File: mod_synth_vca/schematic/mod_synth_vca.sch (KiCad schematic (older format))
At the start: 46 parts, among them J1 Conn_02x08_Odd_Even, J2 AudioJack2, J3 AudioJack2, J4 AudioJack2, J5 AudioJack2, J6 AudioJack2, J7 AudioJack2, J8 Conn_01x10_Female, J9 Conn_01x10_Male, U1 TL074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

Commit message: Modify pcb layout
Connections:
- net PCB_A_CV_A1: now also J9.8 (Pin_8); no longer J9.2 (Pin_2)
- net PCB_A_OUT_A: now also J9.9 (Pin_9); no longer J9.6 (Pin_6)
- net PCB_A_OUT_B: now also J9.2 (Pin_2); no longer J9.7 (Pin_7)
- net PCB_A_VOL_A: now also J9.7 (Pin_7); no longer J9.4 (Pin_4)
- net PCB_A_VOL_B: now also J9.4 (Pin_4); no longer J9.5 (Pin_5)
- net PCB_B_CV_A1: now also J8.8 (Pin_8); no longer J8.2 (Pin_2)
- net PCB_B_OUT_A: now also J8.9 (Pin_9); no longer J8.6 (Pin_6)
- net PCB_B_OUT_B: now also J8.2 (Pin_2); no longer J8.7 (Pin_7)
- net PCB_B_VOL_A: now also J8.7 (Pin_7); no longer J8.4 (Pin_4)
- net PCB_B_VOL_B: now also J8.4 (Pin_4); no longer J8.5 (Pin_5)
- net PCB_B_IN_A: now reaches R12.1, U3.2 (-)
- net PCB_B_IN_A: now also J8.6 (Pin_6); no longer R9.1
- net PCB_B_IN_B: now reaches R11.1, U2.2 (-)
- net PCB_B_IN_B: now also J8.5 (Pin_5); no longer R5.1
- new net PCB_A_IN_A: J9.6 (Pin_6), R9.1
- new net PCB_A_IN_B: J9.5 (Pin_5), R5.1
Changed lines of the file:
@@
-$Comp
-L Amplifier_Operational:TL074 U1
-U 3 1 5D3B02E4
-P 5600 4325
-F 0 "U1" H 5600 4692 50  0000 C CNN
-F 1 "TL074" H 5600 4601 50  0000 C CNN
-F 2 "Package_DIP:DIP-14_W7.62mm_Socket_LongPads" H 5550 4425 50  0001 C CNN
-F 3 "http://www.ti.com/lit/ds/symlink/tl071.pdf" H 5650 4525 50  0001 C CNN
-	3    5600 4325
-	1    0    0    -1
-$EndComp
-$Comp
-L Amplifier_Operational:TL074 U1
-U 4 1 5D3B1A55
-P 7650 4725
-F 0 "U1" H 7650 5092 50  0000 C CNN
-F 1 "TL074" H 7650 5001 50  0000 C CNN
-F 2 "Package_DIP:DIP-14_W7.62mm_Socket_LongPads" H 7600 4825 50  0001 C CNN
-F 3 "http://www.ti.com/lit/ds/symlink/tl071.pdf" H 7700 4925 50  0001 C CNN
-	4    7650 4725
-	1    0    0    -1
-$EndComp
 $Comp
 L Amplifier_Operational:TL074 U1
@@
 	4250 2925 3900 2925
 Wire Wire Line
-	4825 2150 5250 2150
-Wire Wire Line
-	5250 2150 5250 2300
+	4825 2150 5000 2150
 Wire Wire Line
 	5250 2300 5325 2300
@@
 $EndComp
 $Comp
-L power:GND #PWR0124
-U 1 1 5D3DA57A
-P 7175 4350
-F 0 "#PWR0124" H 7175 4100 50  0001 C CNN
-F 1 "GND" H 7180 4177 50  0000 C CNN
-F 2 "" H 7175 4350 50  0001 C CNN
-F 3 "" H 7175 4350 50  0001 C CNN
-	1    7175 4350
-	-1   0    0    1
-$EndComp
-$Comp
 L Connector:AudioJack2 J2
 U 1 1 5D3DA584
@@
 	4200 5800 3850 5800
 Wire Wire Line
-	4775 5025 5200 5025
-Wire Wire Line
-	5200 5025 5200 5175
+	4775 5025 5000 5025
 Wire Wire Line
 	5200 5175 5275 5175
@@
 Wire Wire Line
 	5550 6175 5550 5975
-$Comp
-L power:GND #PWR0125
-U 1 1 5D3DA5C9
-P 5125 4025
-F 0 "#PWR0125" H 5125 3775 50  0001 C CNN
-F 1 "GND" H 5130 3852 50  0000 C CNN
-F 2 "" H 5125 4025 50  0001 C CNN
-F 3 "" H 5125 4025 50  0001 C CNN
-	1    5125 4025
-	-1   0    0    1
-$EndComp
-Wire Wire Line
-	5125 4025 5125 4225
-Wire Wire Line
-	5125 4225 5300 4225
 Wire Wire Line
 	4775 3775 4950 3775
-Wire Wire Line
-	7175 4350 7175 4625
-Wire Wire Line
-	7175 4625 7350 4625
-$Comp
-L Device:D D1
-U 1 1 5D3DA5DC
-P 6200 4475
-F 0 "D1" V 6246 4396 50  0000 R CNN
-F 1 "1N4148" V 6155 4396 50  0000 R CNN
-F 2 "Diode_THT:D_DO-35_SOD27_P7.62mm_Horizontal" H 6200 4475 50  0001 C CNN
-F 3 "~" H 6200 4475 50  0001 C CNN
-	1    6200 4475
-	0    -1   -1   0
-$EndComp
-Wire Wire Line
-	6200 4625 5125 4625
-Wire Wire Line
-	5125 4625 5125 4425
-Wire Wire Line
-	6200 4625 6475 4625
-Wire Wire Line
-	6475 4625 6475 4650
-Connection ~ 6200 4625
 $Comp
 L Device:CP C1
@@
 Connection ~ 8125 5275
 Wire Wire Line
-	7350 4825 7175 4825
-Wire Wire Line
-	7175 4825 7175 5275
-Wire Wire Line
 	7950 4725 8125 4725
 Wire Wire Line
@@
 Wire Wire Line
 	6175 5275 7175 5275
-Wire Wire Line
-	6475 4975 6475 4950
-Wire Wire Line
-	5875 4975 6475 4975
-$Comp
-L Device:D D3
-U 1 1 5D3DA614
-P 6475 4800
-F 0 "D3" V 6521 4721 50  0000 R CNN
-F 1 "1N4148" V 6430 4721 50  0000 R CNN
-F 2 "Diode_THT:D_DO-35_SOD27_P7.62mm_Horizontal" H 6475 4800 50  0001 C CNN
-F 3 "~" H 6475 4800 50  0001 C CNN
-	1    6475 4800
-	0    -1   -1   0
-$EndComp
-$Comp
-L power:+12V #PWR0127
-U 1 1 5D3DA61E
-P 5550 4825
-F 0 "#PWR0127" H 5550 4675 50  0001 C CNN
-F 1 "+12V" H 5565 4998 50  0000 C CNN
-F 2 "" H 5550 4825 50  0001 C CNN
-F 3 "" H 5550 4825 50  0001 C CNN
-	1    5550 4825
-	0    -1   -1   0
-$EndComp
 $Comp
 L power:GND #PWR0128
@@
 	1    0    0    -1
 $EndComp
-$Comp
-L Amplifier_Operational:CA3080 U2
-U 1 1 5D3DA632
-P 5875 5275
-F 0 "U2" H 6219 5321 50  0000 L CNN
-F 1 "CA3080" H 6219 5230 50  0000 L CNN
-F 2 "Package_DIP:DIP-8_W7.62mm_Socket_LongPads" H 5875 5275 50  0001 C CNN
-F 3 "http://www.intersil.com/content/dam/Intersil/documents/ca30/ca3080-a.pdf" H 5875 5375 50  0001 C CNN
-	1    5875 5275
-	1    0    0    -1
-$EndComp
-Wire Wire Line
-	5775 4825 5775 4975
-Wire Wire Line
-	5900 4325 6200 4325
-Wire Wire Line
-	5550 4825 5775 4825
-Wire Wire Line
-	6200 4325 6875 4325
-Wire Wire Line
-	6875 4325 6875 5575
 Wire Wire Line
 	5775 5575 6875 5575
-Connection ~ 6200 4325
 $Comp
 L power:-12V #PWR0129
@@
 Wire Wire Line
 	4900 1550 5175 1550
-Text Label 4950 3775 0    50   ~ 0
-PCB_A_CV_B1
-Connection ~ 5125 4425
-Wire Wire Line
-	5125 4425 5300 4425
 Wire Wire Line
 	4775 4425 4900 4425
-Text Label 4900 4100 0    50   ~ 0
-PCB_B_CV_B1
 Wire Wire Line
 	4900 4100 4900 4425
-Connection ~ 4900 4425
-Wire Wire Line
-	4900 4425 5125 4425
-Text Label 4525 6850 0    50   ~ 0
+Text Label 4525 7450 0    50   ~ 0
 PCB_A_CV_A1
 Text Label 4525 6950 0    50   ~ 0
 PCB_A_CV_B1
-Text Label 3300 6850 2    50   ~ 0
+Text Label 3275 7450 2    50   ~ 0
 PCB_B_CV_A1
 Text Label 3300 6950 2    50   ~ 0
@@
 Wire Wire Line
 	4475 4425 4475 4675
+Text Label 4525 7350 0    50   ~ 0
+PCB_A_VOL_A
 Text Label 4525 7050 0    50   ~ 0
-PCB_A_VOL_A
-Text Label 4525 7150 0    50   ~ 0
 PCB_A_VOL_B
+Text Label 3275 7350 2    50   ~ 0
+PCB_B_VOL_A
 Text Label 3275 7050 2    50   ~ 0
-PCB_B_VOL_A
-Text Label 3275 7150 2    50   ~ 0
 PCB_B_VOL_B
 Wire Wire Line
@@
 Wire Wire Line
 	8275 5275 8275 5500
-Text Label 4525 7250 0    50   ~ 0
+Text Label 4525 7550 0    50   ~ 0
 PCB_A_OUT_A
-Text Label 4525 7350 0    50   ~ 0
+Text Label 4525 6850 0    50   ~ 0
 PCB_A_OUT_B
-Text Label 3275 7250 2    50   ~ 0
+Text Label 3275 7550 2    50   ~ 0
 PCB_B_OUT_A
-Text Label 3275 7350 2    50   ~ 0
+Text Label 3300 6850 2    50   ~ 0
 PCB_B_OUT_B
 Wire Wire Line
@@
 Text Label 8800 5600 0    50   ~ 0
 PCB_A_GND
+Text Label 5000 2100 0    50   ~ 0
+PCB_A_IN_A
+Wire Wire Line
+	5000 2100 5000 2150
+Wire Wire Line
+	5000 4975 5000 5025
+Text Label 5125 2375 2    50   ~ 0
+PCB_B_IN_A
+Text Label 5125 5275 2    50   ~ 0
+PCB_B_IN_B
+Wire Wire Line
+	5125 2375 5250 2375
+Wire Wire Line
+	5250 2375 5250 2300
+Wire Wire Line
+	5200 5175 5200 5275
+Wire Wire Line
+	5200 5275 5125 5275
+Connection ~ 4900 4425
+Text Label 5000 4975 0    50   ~ 0
+PCB_A_IN_B
+Text Label 4900 4100 0    50   ~ 0
+PCB_B_CV_B1
+Text Label 4950 3775 0    50   ~ 0
+PCB_A_CV_B1
+Wire Wire Line
+	6875 4325 6875 5575
+Wire Wire Line
+	5550 4825 5775 4825
+Wire Wire Line
+	5775 4825 5775 4975
+$Comp
+L Amplifier_Operational:CA3080 U2
+U 1 1 5D3DA632
+P 5875 5275
+F 0 "U2" H 6219 5321 50  0000 L CNN
+F 1 "CA3080" H 6219 5230 50  0000 L CNN
+F 2 "Package_DIP:DIP-8_W7.62mm_Socket_LongPads" H 5875 5275 50  0001 C CNN
+F 3 "http://www.intersil.com/content/dam/Intersil/documents/ca30/ca3080-a.pdf" H 5875 5375 50  0001 C CNN
+	1    5875 5275
+	1    0    0    -1
+$EndComp
+$Comp
+L power:+12V #PWR0127
+U 1 1 5D3DA61E
+P 5550 4825
+F 0 "#PWR0127" H 5550 4675 50  0001 C CNN
+F 1 "+12V" H 5565 4998 50  0000 C CNN
+F 2 "" H 5550 4825 50  0001 C CNN
+F 3 "" H 5550 4825 50  0001 C CNN
+	1    5550 4825
+	0    -1   -1   0
+$EndComp
+$Comp
+L Device:D D3
+U 1 1 5D3DA614
+P 6475 4800
+F 0 "D3" V 6521 4721 50  0000 R CNN
+F 1 "1N4148" V 6430 4721 50  0000 R CNN
+F 2 "Diode_THT:D_DO-35_SOD27_P7.62mm_Horizontal" H 6475 4800 50  0001 C CNN
+F 3 "~" H 6475 4800 50  0001 C CNN
+	1    6475 4800
+	0    -1   -1   0
+$EndComp
+Wire Wire Line
+	5875 4975 6475 4975
+Wire Wire Line
+	6475 4975 6475 4950
+Wire Wire Line
+	7175 4825 7175 5275
+Wire Wire Line
+	7350 4825 7175 4825
+Wire Wire Line
+	6475 4625 6475 4650
+Wire Wire Line
+	4900 4425 5125 4425
+Wire Wire Line
+	5125 4425 5300 4425
+Connection ~ 5125 4425
+Wire Wire Line
+	5125 4625 5125 4425
+Wire Wire Line
+	6200 4325 6875 4325
+Wire Wire Line
+	5900 4325 6200 4325
+Connection ~ 6200 4325
+Wire Wire Line
+	6200 4625 6475 4625
+Wire Wire Line
+	6200 4625 5125 4625
+Connection ~ 6200 4625
+$Comp
+L Device:D D1
+U 1 1 5D3DA5DC
+P 6200 4475
+F 0 "D1" V 6246 4396 50  0000 R CNN
+F 1 "1N4148" V 6155 4396 50  0000 R CNN
+F 2 "Diode_THT:D_DO-35_SOD27_P7.62mm_Horizontal" H 6200 4475 50  0001 C CNN
+F 3 "~" H 6200 4475 50  0001 C CNN
+	1    6200 4475
+	0    -1   -1   0
+$EndComp
+Wire Wire Line
+	7175 4625 7350 4625
+Wire Wire Line
+	7175 4350 7175 4625
+Wire Wire Line
+	5125 4225 5300 4225
+Wire Wire Line
+	5125 4025 5125 4225
+$Comp
+L power:GND #PWR0125
+U 1 1 5D3DA5C9
+P 5125 4025
+F 0 "#PWR0125" H 5125 3775 50  0001 C CNN
+F 1 "GND" H 5130 3852 50  0000 C CNN
+F 2 "" H 5125 4025 50  0001 C CNN
+F 3 "" H 5125 4025 50  0001 C CNN
+	1    5125 4025
+	-1   0    0    1
+$EndComp
+$Comp
+L power:GND #PWR0124
+U 1 1 5D3DA57A
+P 7175 4350
+F 0 "#PWR0124" H 7175 4100 50  0001 C CNN
+F 1 "GND" H 7180 4177 50  0000 C CNN
+F 2 "" H 7175 4350 50  0001 C CNN
+F 3 "" H 7175 4350 50  0001 C CNN
+	1    7175 4350
+	-1   0    0    1
+$EndComp
+$Comp
+L Amplifier_Operational:TL074 U1
+U 4 1 5D3B1A55
+P 7650 4725
+F 0 "U1" H 7650 5092 50  0000 C CNN
+F 1 "TL074" H 7650 5001 50  0000 C CNN
+F 2 "Package_DIP:DIP-14_W7.62mm_Socket_LongPads" H 7600 4825 50  0001 C CNN
+F 3 "http://www.ti.com/lit/ds/symlink/tl071.pdf" H 7700 4925 50  0001 C CNN
+	4    7650 4725
+	1    0    0    -1
+$EndComp
+$Comp
+L Amplifier_Operational:TL074 U1
+U 3 1 5D3B02E4
+P 5600 4325
+F 0 "U1" H 5600 4692 50  0000 C CNN
+F 1 "TL074" H 5600 4601 50  0000 C CNN
+F 2 "Package_DIP:DIP-14_W7.62mm_Socket_LongPads" H 5550 4425 50  0001 C CNN
+F 3 "http://www.ti.com/lit/ds/symlink/tl071.pdf" H 5650 4525 50  0001 C CNN
+	3    5600 4325
+	1    0    0    -1
+$EndComp
+Text Label 4525 7250 0    50   ~ 0
+PCB_A_IN_A
+Text Label 4525 7150 0    50   ~ 0
+PCB_A_IN_B
+Text Label 3275 7250 2    50   ~ 0
+PCB_B_IN_A
+Text Label 3275 7150 2    50   ~ 0
+PCB_B_IN_B
+Wire Wire Line
+	3275 7450 3650 7450
+Wire Wire Line
+	4100 7450 4525 7450
+Wire Wire Line
+	4525 7550 4100 7550
+Wire Wire Line
+	3650 7550 3275 7550
 $EndSCHEMATC

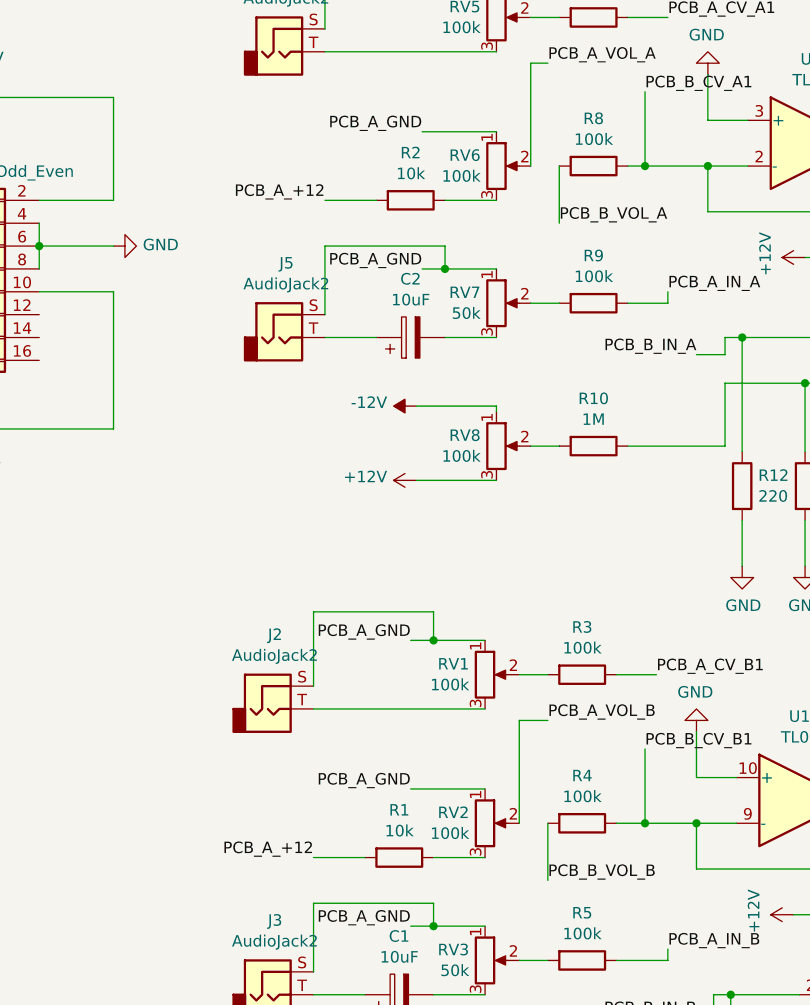
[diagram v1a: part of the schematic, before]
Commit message: Volume resistor should be 20k
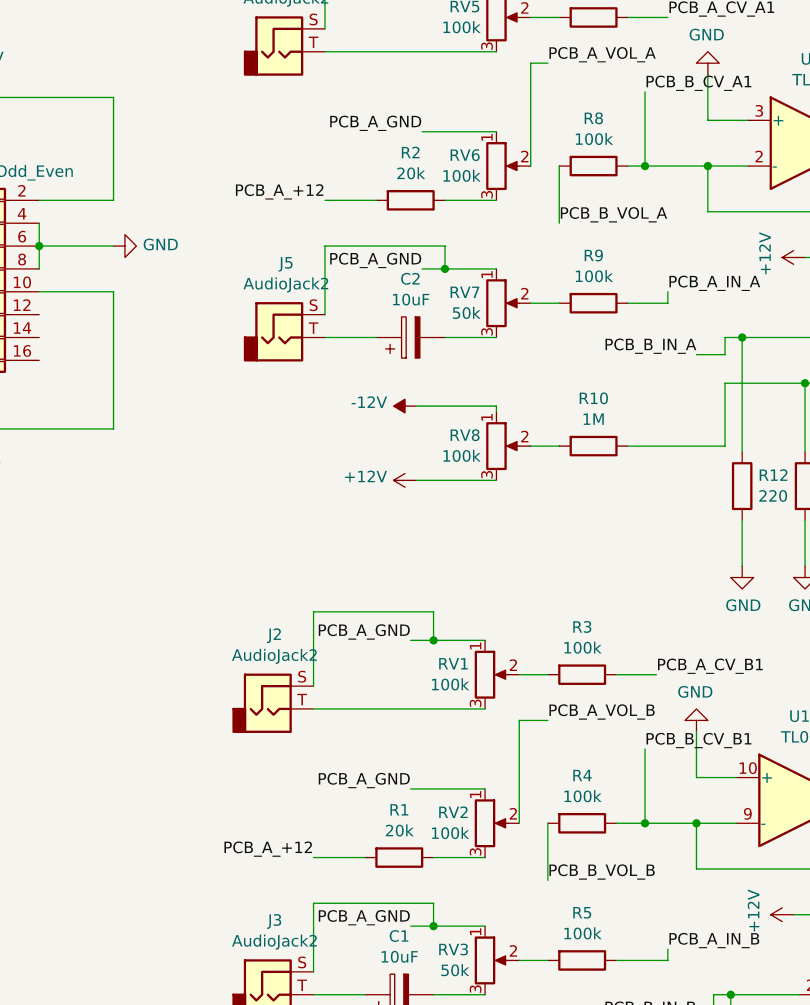
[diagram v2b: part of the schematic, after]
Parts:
- R1, R2: value 10k -> 20k
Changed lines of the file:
@@
 P 3875 1700
 F 0 "R2" V 3668 1700 50  0000 C CNN
-F 1 "10k" V 3759 1700 50  0000 C CNN
+F 1 "20k" V 3759 1700 50  0000 C CNN
 F 2 "Resistor_THT:R_Axial_DIN0207_L6.3mm_D2.5mm_P10.16mm_Horizontal" V 3805 1700 50  0001 C CNN
 F 3 "~" H 3875 1700 50  0001 C CNN
@@
 P 3825 4575
 F 0 "R1" V 3618 4575 50  0000 C CNN
-F 1 "10k" V 3709 4575 50  0000 C CNN
+F 1 "20k" V 3709 4575 50  0000 C CNN
 F 2 "Resistor_THT:R_Axial_DIN0207_L6.3mm_D2.5mm_P10.16mm_Horizontal" V 3755 4575 50  0001 C CNN
 F 3 "~" H 3825 4575 50  0001 C CNN
